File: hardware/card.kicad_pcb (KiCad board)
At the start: 2 copper layers, 143 x 80 mm, 1 part

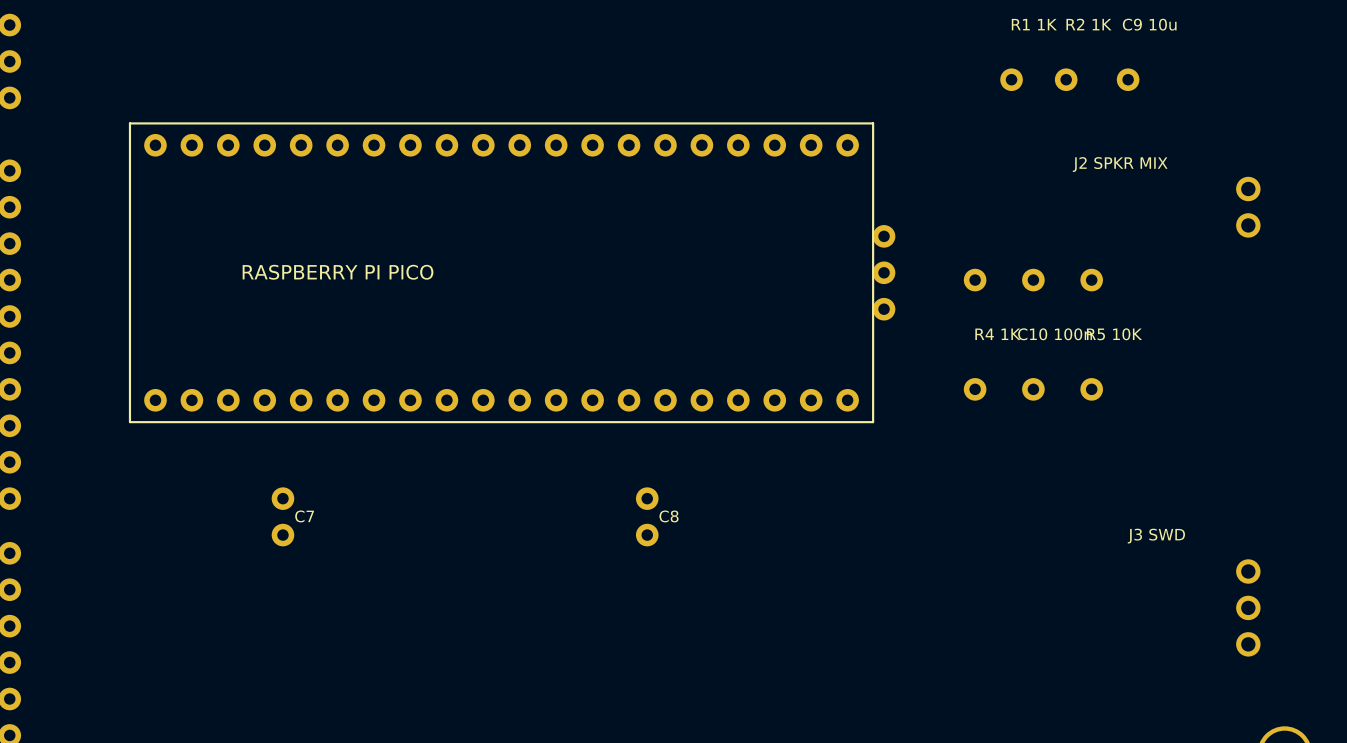
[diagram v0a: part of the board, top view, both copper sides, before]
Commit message: Rebase card on Raspberry Pi Pico W (socketed) with antenna keep-out
The W is pin-compatible, so the change is layout hygiene: removed the
board-level SWD pads and J3 (the Pico WH carries its own JST-SH debug
connector), added a rule-area keep-out under the antenna end (no vias,
no future copper pour; verified 0 vias inside, only pins 19-22 escapes
cross), ANTENNA silk marking, and module socketing noted. Re-routed:
freerouting 999.99, KiCad DRC 0 violations / 0 unconnected. Fab
package and 1:1 plots regenerated. WiFi buys OTA firmware updates and
a live synth-state web view now; the v2 readable-port extension turns
it into a network pipe later.

Co-Authored-By: Claude Fable 5 <noreply@anthropic.com>
Claude-Session: https://claude.ai/code/session_01PB6zhL6oFB9zbtD4W85UDt
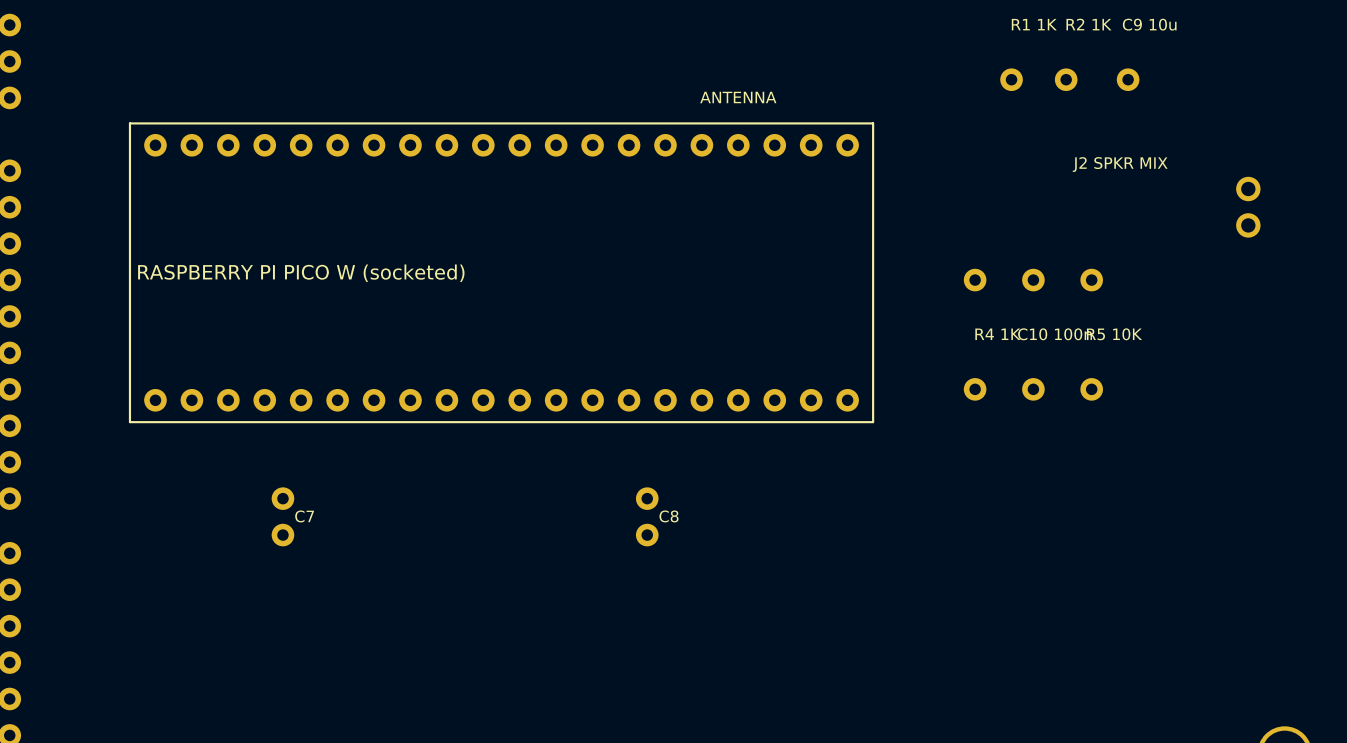
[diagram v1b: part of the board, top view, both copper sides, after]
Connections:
- ? pad 169: SWCLK -> AOL
- ? pad 170: GND -> ASUM
- ? pad 171: SWDIO -> AOR
- ? pad 172: AOL -> ASUM
- ? pad 174: AOR -> AOUT
- ? pad 175: ASUM -> PWM
- ? pad 176: ASUM -> PWMF
- ? pad 177: AOUT -> PWMF
- ? pad 178: PWM -> GND
- ? pad 180: PWMF -> ASUM
- ? pad 181: GND -> AOUT
- ? pad 182: PWMF -> AOUT
- ? pad 183: ASUM -> GND
- ? pad 185: AOUT -> GND
- ? pad 186: GND -> +3V3
- ? pad 187: AOUT -> GND
- ? pad 188: GND -> +3V3
- ? pad 189: SWCLK -> GND
- ? pad 190: GND -> +5V
- ? pad 191: SWDIO -> GND
- ? pad 192: +3V3 -> +5V
- ? pad 194: +3V3 -> +5V
- ? pad 196: +5V -> +3V3
- ? pad 202: +3V3 -> (no net)
- ? pad 203: GND -> (no net)
- ? pad 204: +5V -> (no net)
- ? pad 205: GND -> (no net)
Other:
- board text added: "ANTENNA"
- board text added: "RASPBERRY PI PICO W (socketed)"
- board text removed: "J3 SWD"
- board text removed: "RASPBERRY PI PICO"

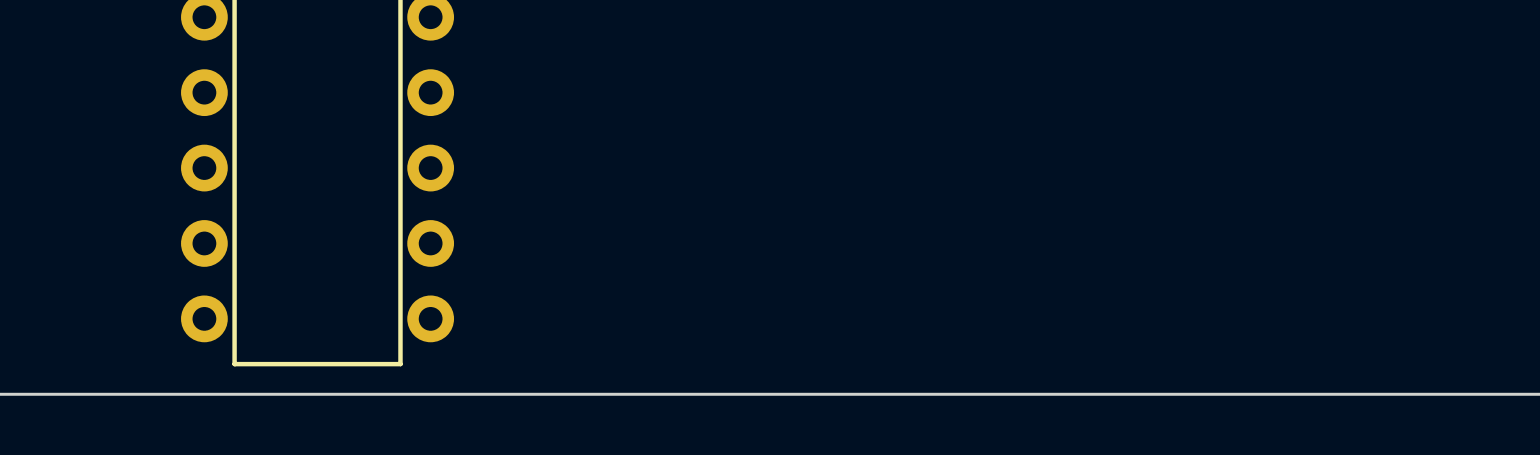
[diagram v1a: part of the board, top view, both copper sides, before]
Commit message: Order prep: memorial notice on both boards, ORDER.md package
Both boards now carry "(c) 2026 David Troy, in memory of Stephen
Troy." on the silkscreen — the card along its bottom edge, the riser
on two lines. Regenerated boards, fab zips, gerbers, and 1:1 plots;
re-verified DRC-clean (0 violations, 0 unconnected on both). ORDER.md
carries the full PCBWay parameter set, the pre-upload checklist, the
per-card BOM, and the bring-up sequence for when the boards arrive.

Co-Authored-By: Claude Fable 5 <noreply@anthropic.com>
Claude-Session: https://claude.ai/code/session_01PB6zhL6oFB9zbtD4W85UDt
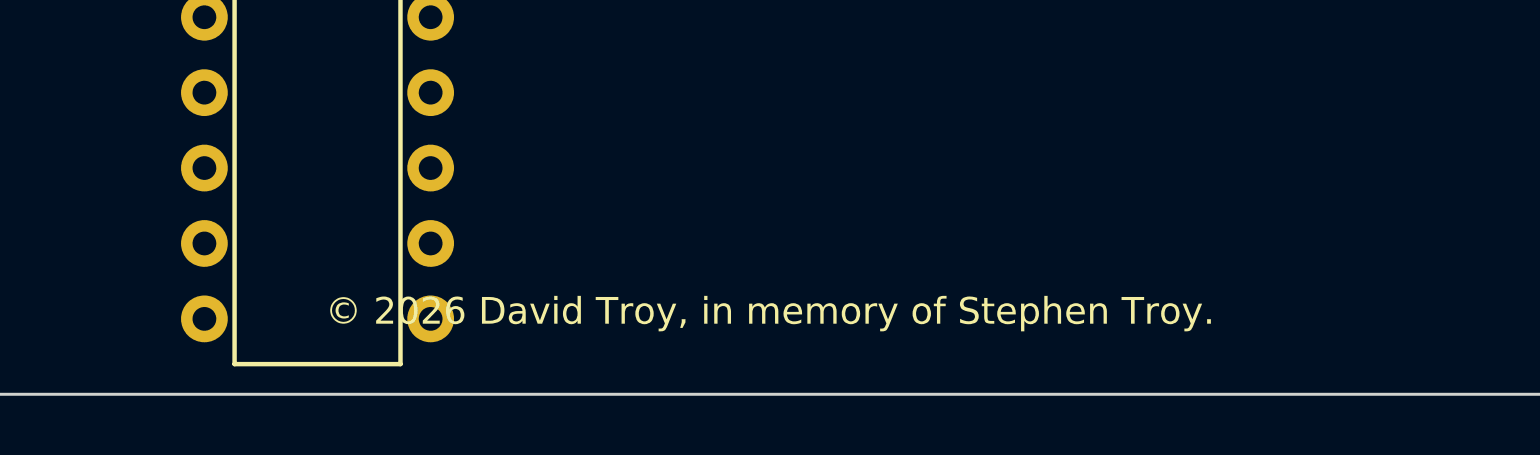
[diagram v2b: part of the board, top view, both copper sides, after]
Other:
- board text added: "© 2026 David Troy, in memory of Stephen Troy."
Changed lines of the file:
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@@
   (gr_text "NS-WSG v1 - NorthStar Advantage wavetable sound card" (at 58.42 2.54) (layer "F.SilkS") (effects (font (size 1.0 1.0) (thickness 0.15))))
   (gr_text "board ID 0xA5 - spec NSWSG.md" (at 58.42 6.096) (layer "F.SilkS") (effects (font (size 0.8 0.8) (thickness 0.15))))
+  (gr_text "© 2026 David Troy, in memory of Stephen Troy." (at 50.8 77.216) (layer "F.SilkS") (effects (font (size 0.9 0.9) (thickness 0.15))))
 )

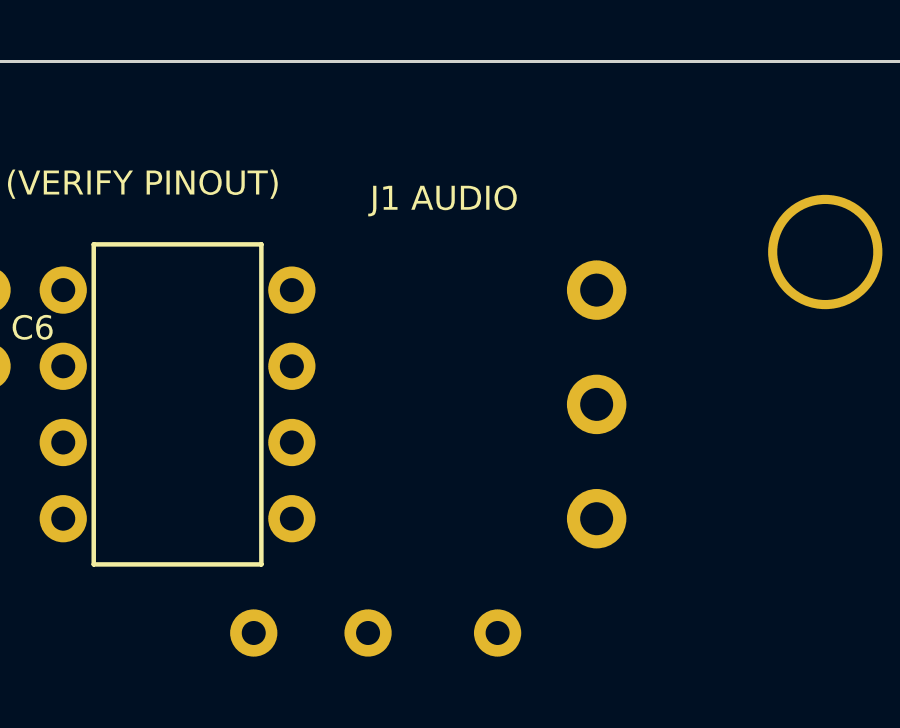
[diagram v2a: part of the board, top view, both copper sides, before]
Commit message: Pre-fab footprint audit: J1 becomes a header, U6 package flagged
Audited every footprint before the order. All standard 0.1"
through-hole except J1, which was an invented 3-pad "jack" matching no
real part — replaced with a plain 1x3 header (pigtail to a panel jack;
real TRS footprint is v2, chosen from a datasheet). U6 check upgraded
to pinout AND package (PT8211 is often SOP-8; adapter-in-socket
fallback documented). Re-routed and re-verified: 0 violations, 0
unconnected. ORDER.md carries the audit results.

Co-Authored-By: Claude Fable 5 <noreply@anthropic.com>
Claude-Session: https://claude.ai/code/session_01PB6zhL6oFB9zbtD4W85UDt
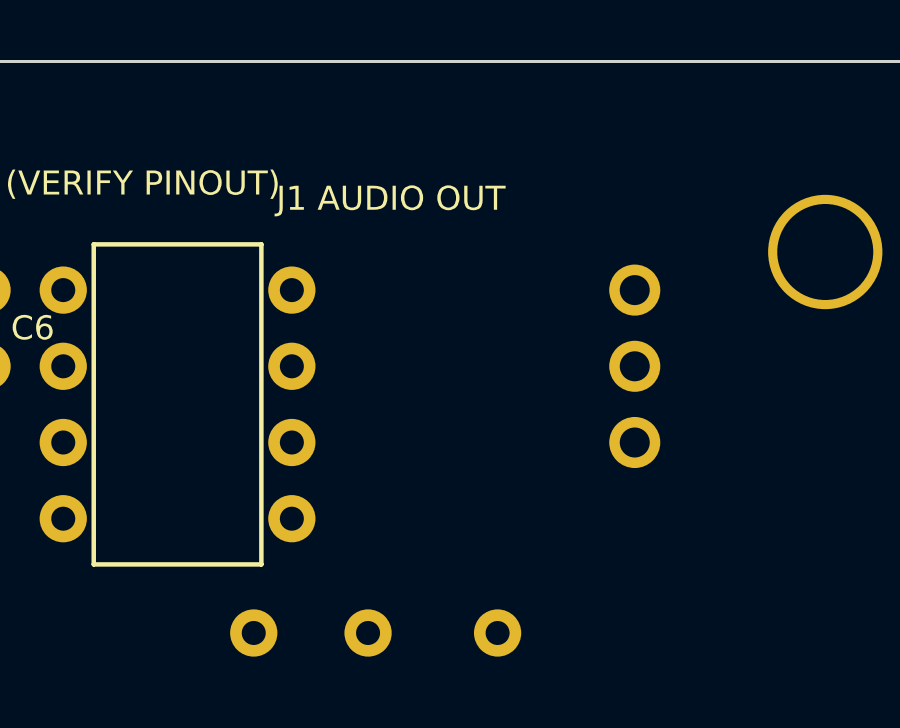
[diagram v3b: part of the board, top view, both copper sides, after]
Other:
- board text added: "J1 AUDIO OUT"
- board text removed: "J1 AUDIO"
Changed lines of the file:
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@@
     (pad "179" thru_hole circle (at 114.808 40.64) (size 1.5748 1.5748) (drill 0.8) (layers "*.Cu" "*.Mask") (net 47 "PWMF"))
     (pad "180" thru_hole circle (at 114.808 48.26) (size 1.5748 1.5748) (drill 0.8) (layers "*.Cu" "*.Mask") (net 45 "ASUM"))
-    (pad "181" thru_hole circle (at 120.65 7.62) (size 1.9812 1.9812) (drill 1.1) (layers "*.Cu" "*.Mask") (net 46 "AOUT"))
-    (pad "182" thru_hole circle (at 120.65 11.43) (size 1.9812 1.9812) (drill 1.1) (layers "*.Cu" "*.Mask") (net 46 "AOUT"))
-    (pad "183" thru_hole circle (at 120.65 15.24) (size 1.9812 1.9812) (drill 1.1) (layers "*.Cu" "*.Mask") (net 1 "GND"))
+    (pad "181" thru_hole circle (at 121.92 7.62) (size 1.7018 1.7018) (drill 1.0) (layers "*.Cu" "*.Mask") (net 46 "AOUT"))
+    (pad "182" thru_hole circle (at 121.92 10.16) (size 1.7018 1.7018) (drill 1.0) (layers "*.Cu" "*.Mask") (net 46 "AOUT"))
+    (pad "183" thru_hole circle (at 121.92 12.7) (size 1.7018 1.7018) (drill 1.0) (layers "*.Cu" "*.Mask") (net 1 "GND"))
     (pad "184" thru_hole circle (at 125.73 34.29) (size 1.7018 1.7018) (drill 1.0) (layers "*.Cu" "*.Mask") (net 46 "AOUT"))
     (pad "185" thru_hole circle (at 125.73 36.83) (size 1.7018 1.7018) (drill 1.0) (layers "*.Cu" "*.Mask") (net 1 "GND"))
@@
   (gr_text "C10 100n" (at 112.268 44.45) (layer "F.SilkS") (effects (font (size 0.8 0.8) (thickness 0.15))))
   (gr_text "R5 10K" (at 116.332 44.45) (layer "F.SilkS") (effects (font (size 0.8 0.8) (thickness 0.15))))
-  (gr_text "J1 AUDIO" (at 115.57 4.572) (layer "F.SilkS") (effects (font (size 0.8 0.8) (thickness 0.15))))
+  (gr_text "J1 AUDIO OUT" (at 113.792 4.572) (layer "F.SilkS") (effects (font (size 0.8 0.8) (thickness 0.15))))
   (gr_text "J2 SPKR MIX" (at 116.84 32.512) (layer "F.SilkS") (effects (font (size 0.8 0.8) (thickness 0.15))))
   (gr_text "C1" (at 15.494 3.81) (layer "F.SilkS") (effects (font (size 0.8 0.8) (thickness 0.15))))

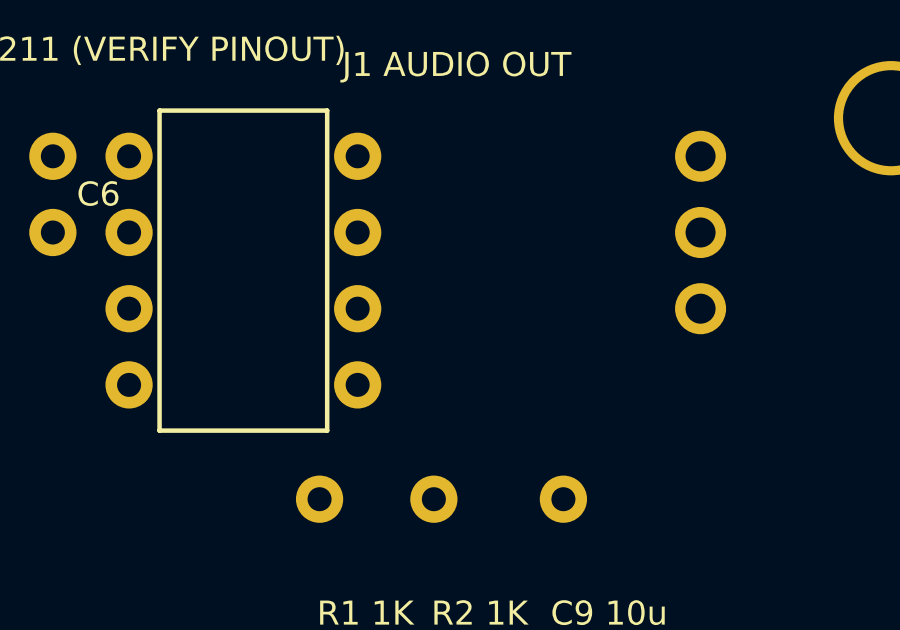
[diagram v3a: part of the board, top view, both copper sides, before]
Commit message: U6 dual position: SOP-8 land beside the DIP socket
PT8211's standard package is SOP-8 (user-confirmed). Nesting SOIC pads
inside the DIP rows failed DRC (6mm cavity is too tight for honest
lands), so U6B is a full-size SOP-8 land beside the DIP position on
the same nets — populate one. Also: injector nudges freerouting's
rare near-min neckdowns (0.15-0.2mm) up to the 0.2mm floor. DRC: 0
violations, 0 unconnected. ORDER.md documents the dual position and
the audio-output options (line-level J1, amp needed for bare 8-ohm
speakers, J2 mix-in for the machine's own speaker).

Co-Authored-By: Claude Fable 5 <noreply@anthropic.com>
Claude-Session: https://claude.ai/code/session_01PB6zhL6oFB9zbtD4W85UDt
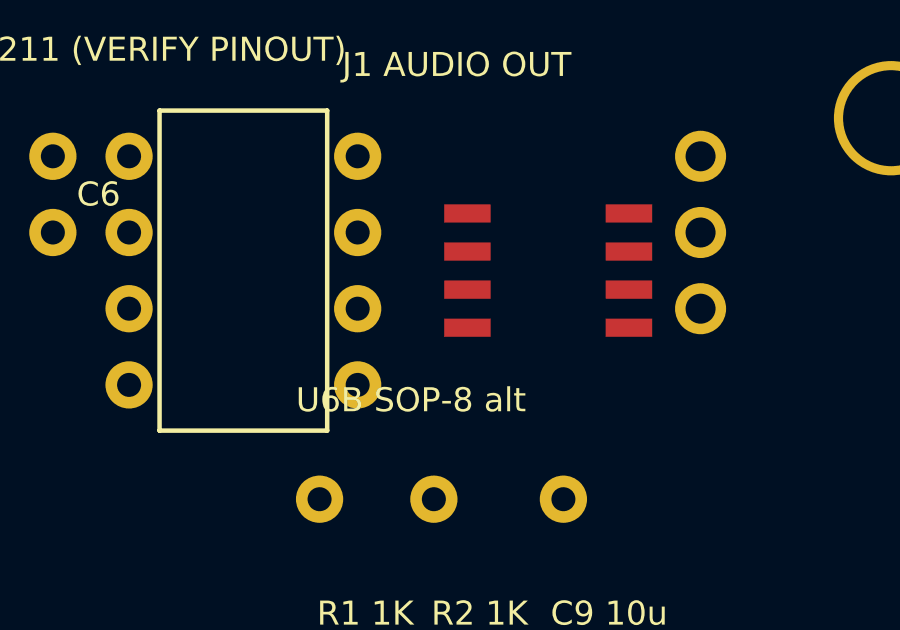
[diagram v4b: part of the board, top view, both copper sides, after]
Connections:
- ? pad 129: GP0 -> BCK
- ? pad 130: (no net) -> AOL
- ? pad 131: GP1 -> WS
- ? pad 132: +5V -> (no net)
- ? pad 133: GND -> DIN
- ? pad 134: GND -> AOR
- ? pad 135: GP2 -> GND
- ? pad 136: (no net) -> +3V3
- ? pad 137: GP3 -> GP0
- ? pad 138: +3V3 -> (no net)
- ? pad 139: GP4 -> GP1
- ? pad 140: (no net) -> +5V
- ? pad 141: GP5 -> GND
- ? pad 142: (no net) -> GND
- ? pad 143: GND -> GP2
- ? pad 144: GND -> (no net)
- ? pad 145: GP6 -> GP3
- ? pad 146: (no net) -> +3V3
- ? pad 147: GP7 -> GP4
- ? pad 149: GP8 -> GP5
- ? pad 151: GP9 -> GND
- ? pad 152: (no net) -> GND
- ? pad 153: GND -> GP6
- ? pad 154: GND -> (no net)
- ? pad 155: GP10 -> GP7
- ? pad 156: PWM -> (no net)
- ? pad 157: GP11 -> GP8
- ? pad 158: DIN -> (no net)
- ? pad 159: GP12 -> GP9
- ? pad 160: WS -> (no net)
- ? pad 161: GP13 -> GND
- ? pad 162: BCK -> GND
- ? pad 163: GND -> GP10
- ? pad 164: GND -> PWM
- ? pad 165: GP14 -> GP11
- ? pad 166: (no net) -> DIN
- ? pad 167: GP15 -> GP12
- ? pad 168: (no net) -> WS
- ? pad 169: AOL -> GP13
- ? pad 170: ASUM -> BCK
- ? pad 171: AOR -> GND
- ? pad 172: ASUM -> GND
- ? pad 173: ASUM -> GP14
- ? pad 174: AOUT -> (no net)
- ? pad 175: PWM -> GP15
- ? pad 176: PWMF -> (no net)
- ? pad 177: PWMF -> AOL
- ? pad 178: GND -> ASUM
- ? pad 179: PWMF -> AOR
- ? pad 181: AOUT -> ASUM
- ? pad 183: GND -> PWM
- ? pad 184: AOUT -> PWMF
- ? pad 185: GND -> PWMF
- ? pad 186: +3V3 -> GND
- ? pad 187: GND -> PWMF
- ? pad 188: +3V3 -> ASUM
- ? pad 189: GND -> AOUT
- ? pad 190: +5V -> AOUT
- ? pad 192: +5V -> AOUT
- ? pad 194: +5V -> +3V3
- ? pad 202: (no net) -> +5V
- ? pad 203: (no net) -> GND
- ? pad 204: (no net) -> +3V3
- ? pad 205: (no net) -> GND
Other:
- board text added: "U6B SOP-8 alt"
